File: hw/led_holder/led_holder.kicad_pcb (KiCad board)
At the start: 2 copper layers, 5.8 x 11.6 mm, 7 parts, among them J1 Conn_01x01, J2 Conn_01x01, J3 Conn_01x01, J4 Conn_01x01

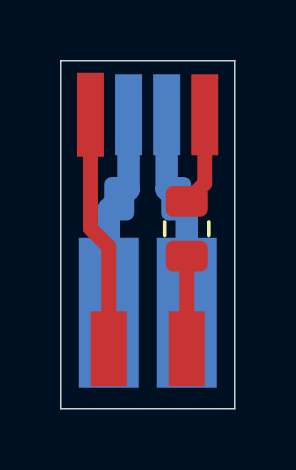
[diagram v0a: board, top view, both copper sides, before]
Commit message: [hw] Move LED holder series resistor
The resistor is moved near the DIN pin of the diode. This change can be
applied the manufactured PCBs by flipping them and soldering the diode
in reverse.
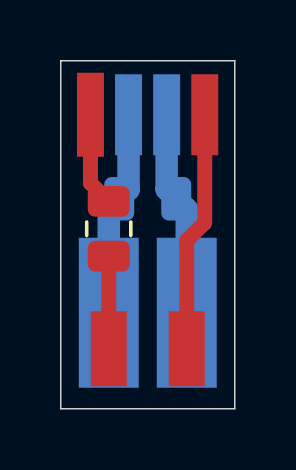
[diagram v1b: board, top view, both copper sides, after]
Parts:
- moved R1 2.60 mm to (121.6, 107.4)
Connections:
- J1 pad 1: Net-(J1-Pad1) -> Net-(D1-Pad1)
- J4 pad 1: Net-(D1-Pad4) -> Net-(J4-Pad1)
- R1 pad 1: Net-(J1-Pad1) -> Net-(J4-Pad1)
- R1 pad 2: Net-(D1-Pad1) -> Net-(D1-Pad4)
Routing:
- net Net-(D1-Pad4): track 8.05 -> 3.14 mm
- net Net-(D1-Pad1): track 3.14 -> 8.05 mm
- net Net-(J4-Pad1): track 0.00 -> 3.09 mm
- net Net-(J1-Pad1): track 3.09 -> 0.00 mm
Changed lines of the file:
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@@
   )
   (setup
-    (last_trace_width 0.25)
+    (last_trace_width 0.5)
     (user_trace_width 0.5)
     (user_trace_width 0.75)
@@
   (net 3 "Net-(D1-Pad4)")
   (net 4 "Net-(D1-Pad1)")
-  (net 5 "Net-(J1-Pad1)")
+  (net 5 "Net-(J4-Pad1)")
   (net_class Default "This is the default net class."
     (clearance 0.2)
@@
     (add_net "Net-(D1-Pad1)")
     (add_net "Net-(D1-Pad4)")
-    (add_net "Net-(J1-Pad1)")
+    (add_net "Net-(J4-Pad1)")
   )
   (module led_holder_footprints:LED_D5.0mm_Edge-4_RGB (layer F.Cu)
@@
       (effects (font (size 1 1) (thickness 0.15)))
     )
+    (fp_line (start -1.23 1.27) (end -1.23 7.37) (layer F.Fab) (width 0.1))
+    (fp_line (start 3.77 1.27) (end 3.77 7.37) (layer F.Fab) (width 0.1))
+    (fp_line (start -1.23 1.27) (end 3.77 1.27) (layer F.Fab) (width 0.1))
+    (fp_line (start 4.17 1.27) (end 4.17 2.27) (layer F.Fab) (width 0.1))
+    (fp_line (start 4.17 2.27) (end 3.77 2.27) (layer F.Fab) (width 0.1))
+    (fp_line (start 3.77 2.27) (end 3.77 1.27) (layer F.Fab) (width 0.1))
+    (fp_line (start 3.77 1.27) (end 4.17 1.27) (layer F.Fab) (width 0.1))
+    (fp_line (start 0 1.27) (end 0 1.27) (layer F.Fab) (width 0.1))
+    (fp_line (start 2.54 1.27) (end 2.54 1.27) (layer F.Fab) (width 0.1))
+    (fp_line (start -1.95 -1.25) (end -1.95 10.2) (layer F.CrtYd) (width 0.05))
+    (fp_line (start -1.95 10.2) (end 4.5 10.2) (layer F.CrtYd) (width 0.05))
+    (fp_line (start 4.5 10.2) (end 4.5 -1.25) (layer F.CrtYd) (width 0.05))
+    (fp_line (start 4.5 -1.25) (end -1.95 -1.25) (layer F.CrtYd) (width 0.05))
     (fp_arc (start 1.27 7.37) (end -1.23 7.37) (angle -180) (layer F.Fab) (width 0.1))
-    (fp_line (start 4.5 -1.25) (end -1.95 -1.25) (layer F.CrtYd) (width 0.05))
-    (fp_line (start 4.5 10.2) (end 4.5 -1.25) (layer F.CrtYd) (width 0.05))
-    (fp_line (start -1.95 10.2) (end 4.5 10.2) (layer F.CrtYd) (width 0.05))
-    (fp_line (start -1.95 -1.25) (end -1.95 10.2) (layer F.CrtYd) (width 0.05))
-    (fp_line (start 2.54 1.27) (end 2.54 1.27) (layer F.Fab) (width 0.1))
-    (fp_line (start 0 1.27) (end 0 1.27) (layer F.Fab) (width 0.1))
-    (fp_line (start 3.77 1.27) (end 4.17 1.27) (layer F.Fab) (width 0.1))
-    (fp_line (start 3.77 2.27) (end 3.77 1.27) (layer F.Fab) (width 0.1))
-    (fp_line (start 4.17 2.27) (end 3.77 2.27) (layer F.Fab) (width 0.1))
-    (fp_line (start 4.17 1.27) (end 4.17 2.27) (layer F.Fab) (width 0.1))
-    (fp_line (start -1.23 1.27) (end 3.77 1.27) (layer F.Fab) (width 0.1))
-    (fp_line (start 3.77 1.27) (end 3.77 7.37) (layer F.Fab) (width 0.1))
-    (fp_line (start -1.23 1.27) (end -1.23 7.37) (layer F.Fab) (width 0.1))
     (pad 1 smd rect (at 0 0 180) (size 0.9 2.7) (layers F.Cu F.Paste F.Mask)
       (net 4 "Net-(D1-Pad1)"))
@@
   )
   (module Resistor_SMD:R_0805_2012Metric (layer F.Cu)
-    (at 124.2 107.4 90)
+    (at 121.6 107.4 90)
     (descr "Resistor SMD 0805 (2012 Metric), square (rectangular) end terminal, IPC_7351 nominal, (Body size source: IPC-SM-782 page 72, https://www.pcb-3d.com/wordpress/wp-content/uploads/ipc-sm-782a_amendment_1_and_2.pdf), generated with kicad-footprint-generator")
     (tags resistor)
@@
       (effects (font (size 1 1) (thickness 0.15)))
     )
+    (fp_line (start -1 0.625) (end -1 -0.625) (layer F.Fab) (width 0.1))
+    (fp_line (start -1 -0.625) (end 1 -0.625) (layer F.Fab) (width 0.1))
+    (fp_line (start 1 -0.625) (end 1 0.625) (layer F.Fab) (width 0.1))
+    (fp_line (start 1 0.625) (end -1 0.625) (layer F.Fab) (width 0.1))
+    (fp_line (start -0.227064 -0.735) (end 0.227064 -0.735) (layer F.SilkS) (width 0.12))
+    (fp_line (start -0.227064 0.735) (end 0.227064 0.735) (layer F.SilkS) (width 0.12))
+    (fp_line (start -1.68 0.95) (end -1.68 -0.95) (layer F.CrtYd) (width 0.05))
+    (fp_line (start -1.68 -0.95) (end 1.68 -0.95) (layer F.CrtYd) (width 0.05))
+    (fp_line (start 1.68 -0.95) (end 1.68 0.95) (layer F.CrtYd) (width 0.05))
     (fp_line (start 1.68 0.95) (end -1.68 0.95) (layer F.CrtYd) (width 0.05))
-    (fp_line (start 1.68 -0.95) (end 1.68 0.95) (layer F.CrtYd) (width 0.05))
-    (fp_line (start -1.68 -0.95) (end 1.68 -0.95) (layer F.CrtYd) (width 0.05))
-    (fp_line (start -1.68 0.95) (end -1.68 -0.95) (layer F.CrtYd) (width 0.05))
-    (fp_line (start -0.227064 0.735) (end 0.227064 0.735) (layer F.SilkS) (width 0.12))
-    (fp_line (start -0.227064 -0.735) (end 0.227064 -0.735) (layer F.SilkS) (width 0.12))
-    (fp_line (start 1 0.625) (end -1 0.625) (layer F.Fab) (width 0.1))
-    (fp_line (start 1 -0.625) (end 1 0.625) (layer F.Fab) (width 0.1))
-    (fp_line (start -1 -0.625) (end 1 -0.625) (layer F.Fab) (width 0.1))
-    (fp_line (start -1 0.625) (end -1 -0.625) (layer F.Fab) (width 0.1))
     (fp_text user %R (at 0 0 90) (layer F.Fab) hide
       (effects (font (size 0.5 0.5) (thickness 0.08)))
     )
     (pad 2 smd roundrect (at 0.9125 0 90) (size 1.025 1.4) (layers F.Cu F.Paste F.Mask) (roundrect_rratio 0.2439014634146341)
-      (net 4 "Net-(D1-Pad1)"))
+      (net 3 "Net-(D1-Pad4)"))
     (pad 1 smd roundrect (at -0.9125 0 90) (size 1.025 1.4) (layers F.Cu F.Paste F.Mask) (roundrect_rratio 0.2439014634146341)
-      (net 5 "Net-(J1-Pad1)"))
+      (net 5 "Net-(J4-Pad1)"))
     (model ${KISYS3DMOD}/Resistor_SMD.3dshapes/R_0805_2012Metric.wrl
       (at (xyz 0 0 0))
@@
       (effects (font (size 1 1) (thickness 0.15)) (justify mirror))
     )
+    (fp_line (start -1 -0.625) (end -1 0.625) (layer B.Fab) (width 0.1))
+    (fp_line (start -1 0.625) (end 1 0.625) (layer B.Fab) (width 0.1))
+    (fp_line (start 1 0.625) (end 1 -0.625) (layer B.Fab) (width 0.1))
+    (fp_line (start 1 -0.625) (end -1 -0.625) (layer B.Fab) (width 0.1))
+    (fp_line (start -0.261252 0.735) (end 0.261252 0.735) (layer B.SilkS) (width 0.12))
+    (fp_line (start -0.261252 -0.735) (end 0.261252 -0.735) (layer B.SilkS) (width 0.12))
+    (fp_line (start -1.7 -0.98) (end -1.7 0.98) (layer B.CrtYd) (width 0.05))
+    (fp_line (start -1.7 0.98) (end 1.7 0.98) (layer B.CrtYd) (width 0.05))
+    (fp_line (start 1.7 0.98) (end 1.7 -0.98) (layer B.CrtYd) (width 0.05))
     (fp_line (start 1.7 -0.98) (end -1.7 -0.98) (layer B.CrtYd) (width 0.05))
-    (fp_line (start 1.7 0.98) (end 1.7 -0.98) (layer B.CrtYd) (width 0.05))
-    (fp_line (start -1.7 0.98) (end 1.7 0.98) (layer B.CrtYd) (width 0.05))
-    (fp_line (start -1.7 -0.98) (end -1.7 0.98) (layer B.CrtYd) (width 0.05))
-    (fp_line (start -0.261252 -0.735) (end 0.261252 -0.735) (layer B.SilkS) (width 0.12))
-    (fp_line (start -0.261252 0.735) (end 0.261252 0.735) (layer B.SilkS) (width 0.12))
-    (fp_line (start 1 -0.625) (end -1 -0.625) (layer B.Fab) (width 0.1))
-    (fp_line (start 1 0.625) (end 1 -0.625) (layer B.Fab) (width 0.1))
-    (fp_line (start -1 0.625) (end 1 0.625) (layer B.Fab) (width 0.1))
-    (fp_line (start -1 -0.625) (end -1 0.625) (layer B.Fab) (width 0.1))
     (pad 2 smd roundrect (at 0.95 0 180) (size 1 1.45) (layers B.Cu B.Paste B.Mask) (roundrect_rratio 0.25)
       (net 2 GND))
@@
     )
     (pad 1 smd rect (at 0 0) (size 1.2 2.5) (layers F.Cu F.Paste F.Mask)
-      (net 5 "Net-(J1-Pad1)"))
+      (net 4 "Net-(D1-Pad1)"))
   )
   (module led_holder_footprints:solder_pad_small (layer F.Cu)
@@
     )
     (pad 1 smd rect (at 0 0) (size 1.2 2.5) (layers F.Cu F.Paste F.Mask)
-      (net 3 "Net-(D1-Pad4)"))
+      (net 5 "Net-(J4-Pad1)"))
   )
   (module led_holder_footprints:solder_pad_big (layer B.Cu)
@@
   (gr_line (start 125.8 101.8) (end 125.8 113.4) (angle 90) (layer Edge.Cuts) (width 0.05))
   (gr_line (start 120 101.8) (end 125.8 101.8) (angle 90) (layer Edge.Cuts) (width 0.05))
-  (segment (start 123.53 103.6) (end 123.53 106.08) (width 0.75) (layer B.Cu) (net 1) (status C00000))
-  (segment (start 123.53 106.08) (end 124.2 106.75) (width 0.75) (layer B.Cu) (net 1) (status C00000))
-  (segment (start 124.2 106.75) (end 124.2 110.2) (width 0.75) (layer B.Cu) (net 1) (status C00000))
-  (segment (start 122.26 103.6) (end 122.26 106.09) (width 0.75) (layer B.Cu) (net 2) (status C00000))
-  (segment (start 122.26 106.09) (end 121.6 106.75) (width 0.75) (layer B.Cu) (net 2) (status C00000))
-  (segment (start 121.6 106.75) (end 121.6 110.2) (width 0.75) (layer B.Cu) (net 2) (status C00000))
-  (segment (start 120.99 103.6) (end 120.99 107.39) (width 0.5) (layer F.Cu) (net 3) (status 400000))
-  (segment (start 121.6 108) (end 121.6 111.4) (width 0.5) (layer F.Cu) (net 3) (status 800000))
-  (segment (start 120.99 107.39) (end 121.6 108) (width 0.5) (layer F.Cu) (net 3))
-  (segment (start 124.8 103.6) (end 124.8 105.8875) (width 0.5) (layer F.Cu) (net 4) (status 400000))
-  (segment (start 124.8 105.8875) (end 124.2 106.4875) (width 0.5) (layer F.Cu) (net 4) (status 800000))
-  (segment (start 124.2 108.3125) (end 124.2 111.4) (width 0.5) (layer F.Cu) (net 5) (status C00000))
+  (segment (start 123.53 103.6) (end 123.53 106.08) (width 0.75) (layer B.Cu) (net 1) (status C00030))
+  (segment (start 123.53 106.08) (end 124.2 106.75) (width 0.75) (layer B.Cu) (net 1) (status C00030))
+  (segment (start 124.2 106.75) (end 124.2 110.2) (width 0.75) (layer B.Cu) (net 1) (status C00030))
+  (segment (start 122.26 103.6) (end 122.26 106.09) (width 0.75) (layer B.Cu) (net 2) (status C00030))
+  (segment (start 122.26 106.09) (end 121.6 106.75) (width 0.75) (layer B.Cu) (net 2) (status C00030))
+  (segment (start 121.6 106.75) (end 121.6 110.2) (width 0.75) (layer B.Cu) (net 2) (status C00030))
+  (segment (start 120.99 105.8775) (end 121.6 106.4875) (width 0.5) (layer F.Cu) (net 3))
+  (segment (start 120.99 103.6) (end 120.99 105.8775) (width 0.5) (layer F.Cu) (net 3))
+  (segment (start 124.8 103.6) (end 124.8 107.2) (width 0.5) (layer F.Cu) (net 4))
+  (segment (start 124.2 107.8) (end 124.2 111.4) (width 0.5) (layer F.Cu) (net 4))
+  (segment (start 124.8 107.2) (end 124.2 107.8) (width 0.5) (layer F.Cu) (net 4))
+  (segment (start 121.6 108.3125) (end 121.6 111.4) (width 0.5) (layer F.Cu) (net 5))
 )
